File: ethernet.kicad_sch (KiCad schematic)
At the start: 51 parts, among them J1 L834-1G1T-S7, U20 KSZ9031RNXCA, Y2 Resonator_25MHz_ABM8G

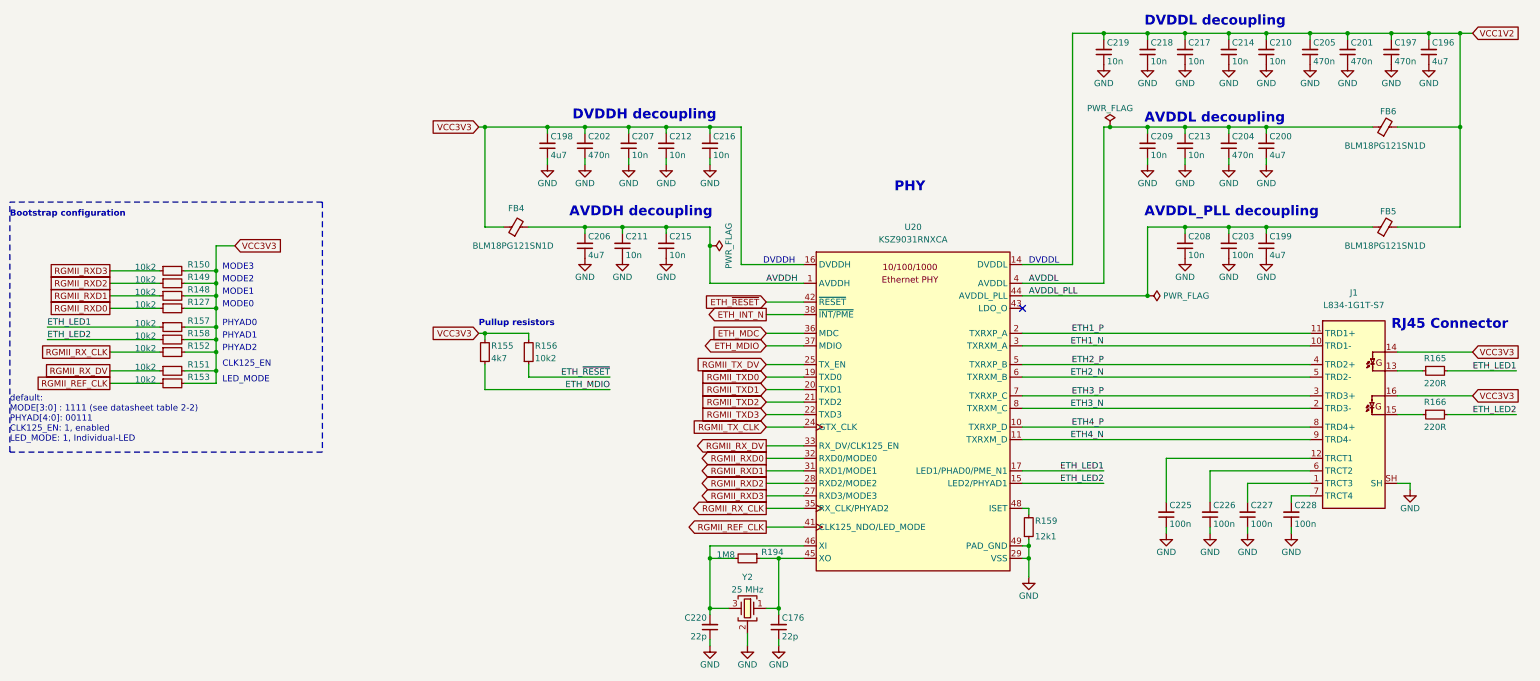
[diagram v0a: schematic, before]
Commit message: [#68236] Update symbols and footprints, clean ERC and DRC
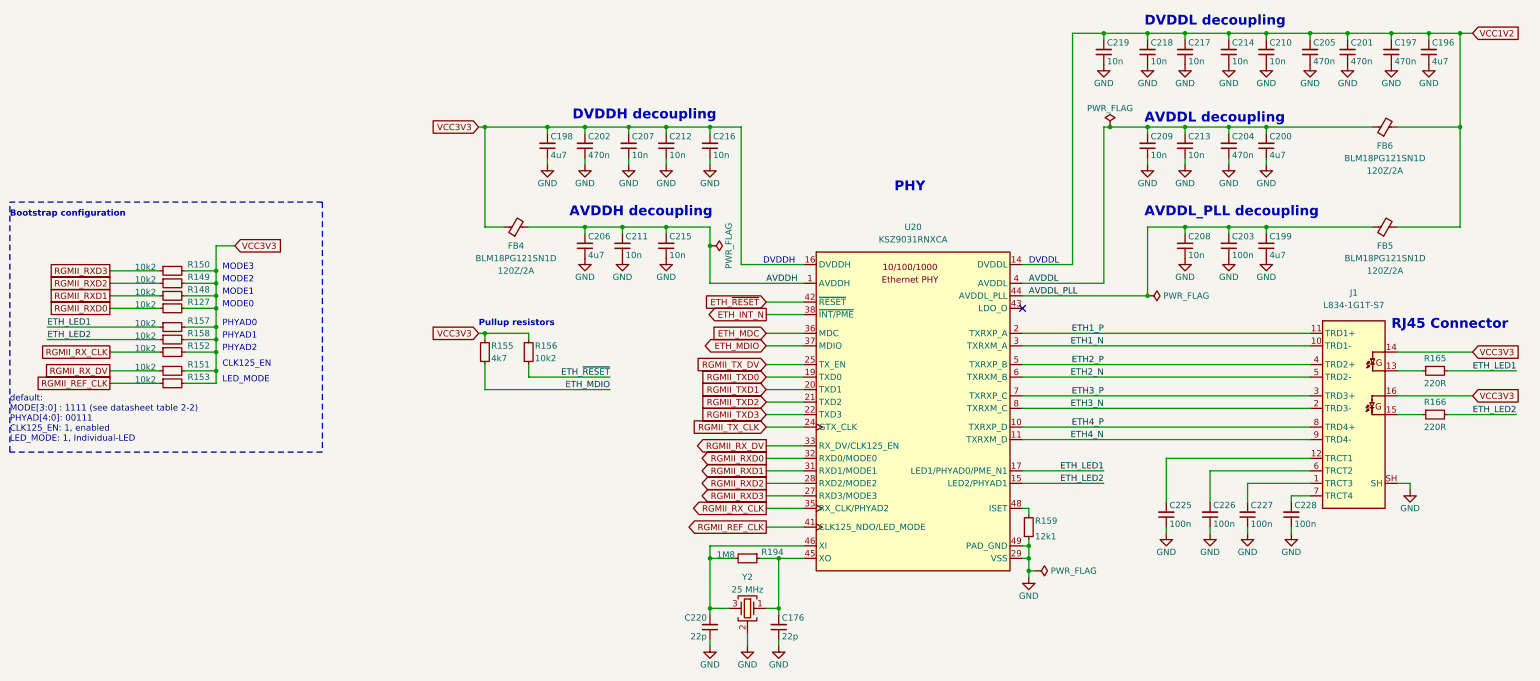
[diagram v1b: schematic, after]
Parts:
- FB4, FB5, FB6: Val (none) -> 120Z/2A
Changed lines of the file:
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@@
   (junction (at 259.08 86.36) (diameter 0) (color 0 0 0 0)
   )
+  (junction (at 242.57 176.53) (diameter 0) (color 0 0 0 0)
+  )
   (junction (at 257.81 67.31) (diameter 0) (color 0 0 0 0)
   )
@@
     (stroke (width 0) (type default))
   )
-  (wire (pts (xy 242.57 173.99) (xy 242.57 177.8))
+  (wire (pts (xy 242.57 173.99) (xy 242.57 176.53))
     (stroke (width 0) (type default))
   )
@@
     (stroke (width 0) (type default))
   )
+  (wire (pts (xy 243.84 176.53) (xy 242.57 176.53))
+    (stroke (width 0) (type default))
+  )
   (wire (pts (xy 140.97 134.62) (xy 140.97 137.16))
     (stroke (width 0) (type default))
@@
     (stroke (width 0) (type default))
   )
+  (wire (pts (xy 242.57 176.53) (xy 242.57 177.8))
+    (stroke (width 0) (type default))
+  )
   (wire (pts (xy 77.47 127) (xy 77.47 129.54))
     (stroke (width 0) (type default))
@@
   )
   (symbol (lib_id "antmicroFerriteBeadsandChips:FB_120Z_2A_Murata-BLM18PG_0603") (at 312.42 86.36 0) (unit 1)
-    (in_bom yes) (on_board yes) (dnp no)
-    (property "Reference" "FB6" (at 315.595 83.185 0)
+    (in_bom yes) (on_board yes) (dnp no) (fields_autoplaced)
+    (property "Reference" "FB6" (at 314.9219 90.17 0)
       (effects (font (size 1.27 1.27)))
     )
@@
       (effects (font (size 1.27 1.27) (thickness 0.15)) (justify left bottom) hide)
     )
-    (property "MPN" "BLM18PG121SN1D" (at 314.96 90.17 0)
+    (property "MPN" "BLM18PG121SN1D" (at 314.9219 92.71 0)
       (effects (font (size 1.27 1.27) (thickness 0.15)))
     )
@@
       (effects (font (size 1.27 1.27) (thickness 0.15)) (justify left bottom) hide)
     )
+    (property "Val" "120Z/2A" (at 314.9219 95.25 0)
+      (effects (font (size 1.27 1.27)))
+    )
+    (property "Current" "" (at 332.74 109.22 0)
+      (effects (font (size 1.27 1.27) (thickness 0.15)) (justify left bottom) hide)
+    )
     (pin "1")
     (pin "2")
@@
   (symbol (lib_id "antmicroFerriteBeadsandChips:FB_120Z_2A_Murata-BLM18PG_0603") (at 312.42 106.68 0) (unit 1)
     (in_bom yes) (on_board yes) (dnp no)
-    (property "Reference" "FB5" (at 315.595 103.505 0)
+    (property "Reference" "FB5" (at 314.96 110.49 0)
       (effects (font (size 1.27 1.27)))
     )
@@
       (effects (font (size 1.27 1.27) (thickness 0.15)) (justify left bottom) hide)
     )
-    (property "MPN" "BLM18PG121SN1D" (at 314.96 110.49 0)
+    (property "MPN" "BLM18PG121SN1D" (at 314.96 113.03 0)
       (effects (font (size 1.27 1.27) (thickness 0.15)))
     )
@@
       (effects (font (size 1.27 1.27) (thickness 0.15)) (justify left bottom) hide)
     )
+    (property "Val" "120Z/2A" (at 314.96 115.57 0)
+      (effects (font (size 1.27 1.27)))
+    )
+    (property "Current" "" (at 332.74 129.54 0)
+      (effects (font (size 1.27 1.27) (thickness 0.15)) (justify left bottom) hide)
+    )
     (pin "1")
     (pin "2")
@@
   )
   (symbol (lib_id "antmicroFerriteBeadsandChips:FB_120Z_2A_Murata-BLM18PG_0603") (at 135.89 106.68 0) (unit 1)
-    (in_bom yes) (on_board yes) (dnp no)
-    (property "Reference" "FB4" (at 138.43 102.87 0)
+    (in_bom yes) (on_board yes) (dnp no) (fields_autoplaced)
+    (property "Reference" "FB4" (at 138.3919 110.49 0)
       (effects (font (size 1.27 1.27)))
     )
@@
       (effects (font (size 1.27 1.27) (thickness 0.15)) (justify left bottom) hide)
     )
-    (property "MPN" "BLM18PG121SN1D" (at 137.795 110.49 0)
+    (property "MPN" "BLM18PG121SN1D" (at 138.3919 113.03 0)
       (effects (font (size 1.27 1.27) (thickness 0.15)))
     )
@@
       (effects (font (size 1.27 1.27) (thickness 0.15)) (justify left bottom) hide)
     )
+    (property "Val" "120Z/2A" (at 138.3919 115.57 0)
+      (effects (font (size 1.27 1.27)))
+    )
+    (property "Current" "" (at 156.21 129.54 0)
+      (effects (font (size 1.27 1.27) (thickness 0.15)) (justify left bottom) hide)
+    )
     (pin "1")
     (pin "2")
@@
         )
       )
+    )
+  )
+  (symbol (lib_id "antmicropower:PWR_FLAG") (at 243.84 176.53 270) (unit 1)
+    (in_bom yes) (on_board yes) (dnp no) (fields_autoplaced)
+    (property "Reference" "#FLG01" (at 245.745 176.53 0)
+      (effects (font (size 1.27 1.27)) hide)
+    )
+    (property "Value" "PWR_FLAG" (at 247.015 176.5299 90)
+      (effects (font (size 1.27 1.27)) (justify left))
+    )
+    (property "Footprint" "" (at 243.84 176.53 0)
+      (effects (font (size 1.27 1.27)) hide)
+    )
+    (property "Datasheet" "" (at 243.84 176.53 0)
+      (effects (font (size 1.27 1.27)) hide)
+    )
+    (pin "1")
+    (instances
+      (project "artix-dc-scm"
+        (path "/f3cd042e-9a46-4397-9768-c62eb1c291be/00000000-0000-0000-0000-000060570c04"
+          (reference "#FLG01") (unit 1)
+        )
+      )

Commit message: pcb layout progress
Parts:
- added R198, R199, R200, R201, R202, R203: 33, Resistor_SMD:R_0402_1005Metric, symbol Device:R_Small
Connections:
- net RGMII_TXD0: now also R199.1; no longer U20.19 (TXD0)
- net RGMII_TXD1: now also R200.1; no longer U20.20 (TXD1)
- net RGMII_TXD2: now also R201.1; no longer U20.21 (TXD2)
- net RGMII_TXD3: now also R202.1; no longer U20.22 (TXD3)
- net RGMII_TX_CLK: now also R203.1; no longer U20.24 (GTX_CLK)
- net RGMII_TX_DV: now also R198.1; no longer U20.25 (TX_EN)
- new net RGMII_CLK_PHY: R203.2, U20.24 (GTX_CLK)
- new net RGMII_TXD0_PHY: R199.2, U20.19 (TXD0)
- new net RGMII_TXD1_PHY: R200.2, U20.20 (TXD1)
- new net RGMII_TXD2_PHY: R201.2, U20.21 (TXD2)
- new net RGMII_TXD3_PHY: R202.2, U20.22 (TXD3)
- new net RGMII_TX_EN_PHY: R198.2, U20.25 (TX_EN)
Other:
- moved on the sheet: R155, R156

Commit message: a lot of routing and almost all caps of the fpga are placed down
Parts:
- C176, C196, C197, C198, C199, C200, C201, C202, C203, C204, C205, C206, C207, C208, C209, C210, C211, C212, C213, C214, C215, C216, C217, C218, C219, C220, C225, C226, C227, C228: footprint antmicro-footprints:C_0402_1005Metric -> Capacitor_SMD:C_0402_1005Metric
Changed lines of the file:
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@@
 			)
 		)
-		(property "Footprint" "antmicro-footprints:C_0402_1005Metric"
+		(property "Footprint" "Capacitor_SMD:C_0402_1005Metric"
 			(at 278.13 72.39 0)
 			(hide yes)
@@
 			)
 		)
-		(property "Footprint" "antmicro-footprints:C_0402_1005Metric"
+		(property "Footprint" "Capacitor_SMD:C_0402_1005Metric"
 			(at 270.51 72.39 0)
 			(hide yes)
@@
 			)
 		)
-		(property "Footprint" "antmicro-footprints:C_0402_1005Metric"
+		(property "Footprint" "Capacitor_SMD:C_0402_1005Metric"
 			(at 254 72.39 0)
 			(hide yes)
@@
 			)
 		)
-		(property "Footprint" "antmicro-footprints:C_0402_1005Metric"
+		(property "Footprint" "Capacitor_SMD:C_0402_1005Metric"
 			(at 261.62 72.39 0)
 			(hide yes)
@@
 			)
 		)
-		(property "Footprint" "antmicro-footprints:C_0402_1005Metric"
+		(property "Footprint" "Capacitor_SMD:C_0402_1005Metric"
 			(at 261.62 92.71 0)
 			(hide yes)
@@
 			)
 		)
-		(property "Footprint" "antmicro-footprints:C_0402_1005Metric"
+		(property "Footprint" "Capacitor_SMD:C_0402_1005Metric"
 			(at 278.13 92.71 0)
 			(hide yes)
@@
 			)
 		)
-		(property "Footprint" "antmicro-footprints:C_0402_1005Metric"
+		(property "Footprint" "Capacitor_SMD:C_0402_1005Metric"
 			(at 270.51 92.71 0)
 			(hide yes)
@@
 			)
 		)
-		(property "Footprint" "antmicro-footprints:C_0402_1005Metric"
+		(property "Footprint" "Capacitor_SMD:C_0402_1005Metric"
 			(at 279.4 53.34 0)
 			(hide yes)
@@
 			)
 		)
-		(property "Footprint" "antmicro-footprints:C_0402_1005Metric"
+		(property "Footprint" "Capacitor_SMD:C_0402_1005Metric"
 			(at 270.51 53.34 0)
 			(hide yes)
@@
 			)
 		)
-		(property "Footprint" "antmicro-footprints:C_0402_1005Metric"
+		(property "Footprint" "Capacitor_SMD:C_0402_1005Metric"
 			(at 295.91 53.34 0)
 			(hide yes)
@@
 			)
 		)
-		(property "Footprint" "antmicro-footprints:C_0402_1005Metric"
+		(property "Footprint" "Capacitor_SMD:C_0402_1005Metric"
 			(at 287.02 53.34 0)
 			(hide yes)
@@
 			)
 		)
-		(property "Footprint" "antmicro-footprints:C_0402_1005Metric"
+		(property "Footprint" "Capacitor_SMD:C_0402_1005Metric"
 			(at 172.72 92.71 0)
 			(hide yes)
@@
 			)
 		)
-		(property "Footprint" "antmicro-footprints:C_0402_1005Metric"
+		(property "Footprint" "Capacitor_SMD:C_0402_1005Metric"
 			(at 303.53 53.34 0)
 			(hide yes)
@@
 			)
 		)
-		(property "Footprint" "antmicro-footprints:C_0402_1005Metric"
+		(property "Footprint" "Capacitor_SMD:C_0402_1005Metric"
 			(at 336.55 53.34 0)
 			(hide yes)
@@
 			)
 		)
-		(property "Footprint" "antmicro-footprints:C_0402_1005Metric"
+		(property "Footprint" "Capacitor_SMD:C_0402_1005Metric"
 			(at 328.93 53.34 0)
 			(hide yes)
@@
 			)
 		)
-		(property "Footprint" "antmicro-footprints:C_0402_1005Metric"
+		(property "Footprint" "Capacitor_SMD:C_0402_1005Metric"
 			(at 320.04 53.34 0)
 			(hide yes)
@@
 			)
 		)
-		(property "Footprint" "antmicro-footprints:C_0402_1005Metric"
+		(property "Footprint" "Capacitor_SMD:C_0402_1005Metric"
 			(at 312.42 53.34 0)
 			(hide yes)
@@
 			)
 		)
-		(property "Footprint" "antmicro-footprints:C_0402_1005Metric"
+		(property "Footprint" "Capacitor_SMD:C_0402_1005Metric"
 			(at 181.61 92.71 0)
 			(hide yes)
@@
 			)
 		)
-		(property "Footprint" "antmicro-footprints:C_0402_1005Metric"
+		(property "Footprint" "Capacitor_SMD:C_0402_1005Metric"
 			(at 165.1 92.71 0)
 			(hide yes)
@@
 			)
 		)
-		(property "Footprint" "antmicro-footprints:C_0402_1005Metric"
+		(property "Footprint" "Capacitor_SMD:C_0402_1005Metric"
 			(at 157.48 72.39 0)
 			(hide yes)
@@
 			)
 		)
-		(property "Footprint" "antmicro-footprints:C_0402_1005Metric"
+		(property "Footprint" "Capacitor_SMD:C_0402_1005Metric"
 			(at 165.1 72.39 0)
 			(hide yes)
@@
 			)
 		)
-		(property "Footprint" "antmicro-footprints:C_0402_1005Metric"
+		(property "Footprint" "Capacitor_SMD:C_0402_1005Metric"
 			(at 181.61 72.39 0)
 			(hide yes)
@@
 			)
 		)
-		(property "Footprint" "antmicro-footprints:C_0402_1005Metric"
+		(property "Footprint" "Capacitor_SMD:C_0402_1005Metric"
 			(at 190.5 72.39 0)
 			(hide yes)
@@
 			)
 		)
-		(property "Footprint" "antmicro-footprints:C_0402_1005Metric"
+		(property "Footprint" "Capacitor_SMD:C_0402_1005Metric"
 			(at 173.99 72.39 0)
 			(hide yes)
@@
 			)
 		)
-		(property "Footprint" "antmicro-footprints:C_0402_1005Metric"
+		(property "Footprint" "Capacitor_SMD:C_0402_1005Metric"
 			(at 179.07 170.18 0)
 			(hide yes)
@@
 			)
 		)
-		(property "Footprint" "antmicro-footprints:C_0402_1005Metric"
+		(property "Footprint" "Capacitor_SMD:C_0402_1005Metric"
 			(at 165.1 170.18 0)
 			(hide yes)
@@
 			)
 		)
-		(property "Footprint" "antmicro-footprints:C_0402_1005Metric"
+		(property "Footprint" "Capacitor_SMD:C_0402_1005Metric"
 			(at 299.72 147.32 0)
 			(hide yes)
@@
 			)
 		)
-		(property "Footprint" "antmicro-footprints:C_0402_1005Metric"
+		(property "Footprint" "Capacitor_SMD:C_0402_1005Metric"
 			(at 292.1 147.32 0)
 			(hide yes)
@@
 			)
 		)
-		(property "Footprint" "antmicro-footprints:C_0402_1005Metric"
+		(property "Footprint" "Capacitor_SMD:C_0402_1005Metric"
 			(at 283.21 147.32 0)
 			(hide yes)
@@
 			)
 		)
-		(property "Footprint" "antmicro-footprints:C_0402_1005Metric"
+		(property "Footprint" "Capacitor_SMD:C_0402_1005Metric"
 			(at 308.61 147.32 0)
 			(hide yes)

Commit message: a lot of poin swaps
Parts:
- C197, C201, C202, C204, C205: MPN C1005X5R1E474M050BB -> GXT155C80J474KE01D; Manufacturer TDK -> Murata Electronics
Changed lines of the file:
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@@
 			)
 		)
-		(property "Datasheet" "https://product.tdk.com/en/search/capacitor/ceramic/mlcc/info?part_no=C1005X5R1E474M050BB"
+		(property "Datasheet" ""
 			(at 267.97 72.39 0)
 			(hide yes)
@@
 			)
 		)
-		(property "Description" "SMD Multilayer Ceramic Capacitor, 0.47 µF, 25 V, 0402 [1005 Metric], ± 20%, X5R, C"
+		(property "Description" "Multilayer Ceramic Capacitors MLCC - SMD/SMT 0402 6.3VDC 0.47uF 10% X6S AEC-Q200"
 			(at 283.21 92.71 0)
 			(hide yes)
@@
 			)
 		)
-		(property "Manufacturer" "TDK"
+		(property "Manufacturer" "Murata Electronics"
 			(at 262.89 72.39 0)
 			(hide yes)
@@
 			)
 		)
-		(property "MPN" "C1005X5R1E474M050BB"
+		(property "MPN" "GXT155C80J474KE01D"
 			(at 265.43 72.39 0)
 			(hide yes)
@@
 			)
 		)
-		(property "Datasheet" "https://product.tdk.com/en/search/capacitor/ceramic/mlcc/info?part_no=C1005X5R1E474M050BB"
+		(property "Datasheet" ""
 			(at 331.47 53.34 0)
 			(hide yes)
@@
 			)
 		)
-		(property "Description" "SMD Multilayer Ceramic Capacitor, 0.47 µF, 25 V, 0402 [1005 Metric], ± 20%, X5R, C"
+		(property "Description" "Multilayer Ceramic Capacitors MLCC - SMD/SMT 0402 6.3VDC 0.47uF 10% X6S AEC-Q200"
 			(at 316.23 73.66 0)
 			(hide yes)
@@
 			)
 		)
-		(property "Manufacturer" "TDK"
+		(property "Manufacturer" "Murata Electronics"
 			(at 336.55 53.34 0)
 			(hide yes)
@@
 			)
 		)
-		(property "MPN" "C1005X5R1E474M050BB"
+		(property "MPN" "GXT155C80J474KE01D"
 			(at 334.01 53.34 0)
 			(hide yes)
@@
 			)
 		)
-		(property "Datasheet" "https://product.tdk.com/en/search/capacitor/ceramic/mlcc/info?part_no=C1005X5R1E474M050BB"
+		(property "Datasheet" ""
 			(at 322.58 53.34 0)
 			(hide yes)
@@
 			)
 		)
-		(property "Description" "SMD Multilayer Ceramic Capacitor, 0.47 µF, 25 V, 0402 [1005 Metric], ± 20%, X5R, C"
+		(property "Description" "Multilayer Ceramic Capacitors MLCC - SMD/SMT 0402 6.3VDC 0.47uF 10% X6S AEC-Q200"
 			(at 307.34 73.66 0)
 			(hide yes)
@@
 			)
 		)
-		(property "Manufacturer" "TDK"
+		(property "Manufacturer" "Murata Electronics"
 			(at 327.66 53.34 0)
 			(hide yes)
@@
 			)
 		)
-		(property "MPN" "C1005X5R1E474M050BB"
+		(property "MPN" "GXT155C80J474KE01D"
 			(at 325.12 53.34 0)
 			(hide yes)
@@
 			)
 		)
-		(property "Datasheet" "https://product.tdk.com/en/search/capacitor/ceramic/mlcc/info?part_no=C1005X5R1E474M050BB"
+		(property "Datasheet" ""
 			(at 314.96 53.34 0)
 			(hide yes)
@@
 			)
 		)
-		(property "Description" "SMD Multilayer Ceramic Capacitor, 0.47 µF, 25 V, 0402 [1005 Metric], ± 20%, X5R, C"
+		(property "Description" "Multilayer Ceramic Capacitors MLCC - SMD/SMT 0402 6.3VDC 0.47uF 10% X6S AEC-Q200"
 			(at 299.72 73.66 0)
 			(hide yes)
@@
 			)
 		)
-		(property "Manufacturer" "TDK"
+		(property "Manufacturer" "Murata Electronics"
 			(at 320.04 53.34 0)
 			(hide yes)
@@
 			)
 		)
-		(property "MPN" "C1005X5R1E474M050BB"
+		(property "MPN" "GXT155C80J474KE01D"
 			(at 317.5 53.34 0)
 			(hide yes)
@@
 			)
 		)
-		(property "Datasheet" "https://product.tdk.com/en/search/capacitor/ceramic/mlcc/info?part_no=C1005X5R1E474M050BB"
+		(property "Datasheet" ""
 			(at 167.64 72.39 0)
 			(hide yes)
@@
 			)
 		)
-		(property "Description" "SMD Multilayer Ceramic Capacitor, 0.47 µF, 25 V, 0402 [1005 Metric], ± 20%, X5R, C"
+		(property "Description" "Multilayer Ceramic Capacitors MLCC - SMD/SMT 0402 6.3VDC 0.47uF 10% X6S AEC-Q200"
 			(at 152.4 92.71 0)
 			(hide yes)
@@
 			)
 		)
-		(property "Manufacturer" "TDK"
+		(property "Manufacturer" "Murata Electronics"
 			(at 172.72 72.39 0)
 			(hide yes)
@@
 			)
 		)
-		(property "MPN" "C1005X5R1E474M050BB"
+		(property "MPN" "GXT155C80J474KE01D"
 			(at 170.18 72.39 0)
 			(hide yes)

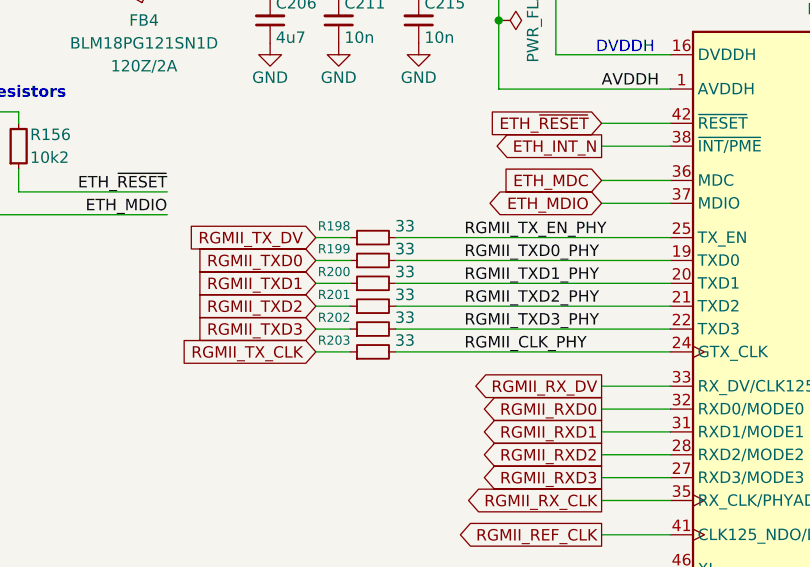
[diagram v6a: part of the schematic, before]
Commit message: bom changes
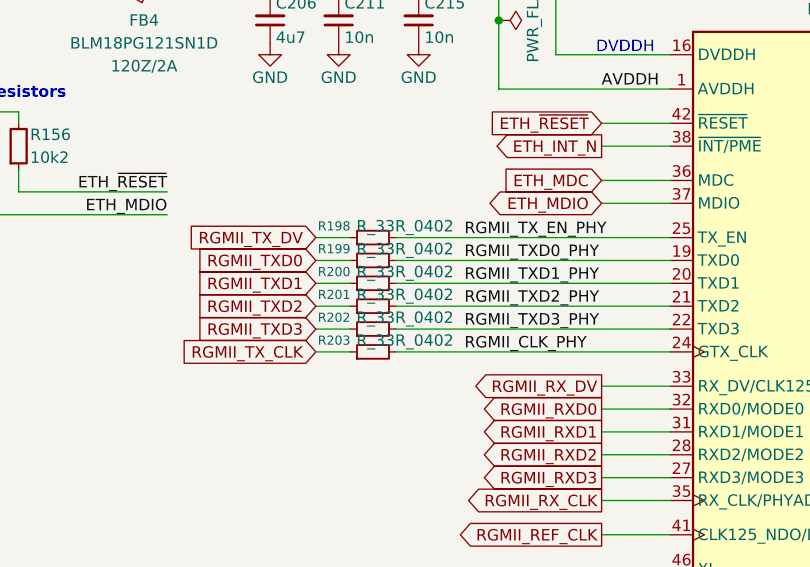
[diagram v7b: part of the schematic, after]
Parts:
- R198, R199, R200, R201, R202, R203: value 33 -> R_33R_0402

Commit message: version 1.0 complete
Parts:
- R155: MPN CR0402-FX-4701GLF -> RC0402FR-7D4K7L; Manufacturer Bourns -> YAGEO
- R194: MPN CR0402-FX-1804GLF -> RC0402FR-131M8L; Manufacturer Bourns -> YAGEO
- R198, R199, R200, R201, R202, R203: MPN (none) -> MCS04020C3309FE000; Manufacturer (none) -> Vishay / Beyschlag
